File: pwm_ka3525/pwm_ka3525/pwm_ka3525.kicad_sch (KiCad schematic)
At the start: 17 parts, among them J1 shutdown, J2 Conn_01x03, J3 Conn_01x03, J4 Conn_01x02, U1 UC3525

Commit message: actualizacion
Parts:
- added C3: 0.1uF, Capacitor_THT:C_Disc_D7.5mm_W2.5mm_P5.00mm, symbol Device:C
- frec1: value 200k -> 150k
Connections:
- net +12V: now also C3.1
- net GND: now also C3.2
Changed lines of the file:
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@@
+    (stroke (width 0) (type default))
+  )
+  (wire (pts (xy 218.44 73.66) (xy 218.44 76.2))
     (stroke (width 0) (type default))
   )
@@
   )
   (wire (pts (xy 105.41 97.79) (xy 105.41 104.14))
+    (stroke (width 0) (type default))
+  )
+  (wire (pts (xy 218.44 83.82) (xy 218.44 85.09))
     (stroke (width 0) (type default))
   )
@@
         (path "/ea49c21e-f169-43d4-aeb6-478b59f13c59"
           (reference "#PWR09") (unit 1)
+        )
+      )
+    )
+  )
+  (symbol (lib_id "Device:C") (at 218.44 80.01 0) (unit 1)
+    (in_bom yes) (on_board yes) (dnp no) (fields_autoplaced)
+    (property "Reference" "C3" (at 222.25 79.375 0)
+      (effects (font (size 1.27 1.27)) (justify left))
+    )
+    (property "Value" "0.1uF" (at 222.25 81.915 0)
+      (effects (font (size 1.27 1.27)) (justify left))
+    )
+    (property "Footprint" "Capacitor_THT:C_Disc_D7.5mm_W2.5mm_P5.00mm" (at 219.4052 83.82 0)
+      (effects (font (size 1.27 1.27)) hide)
+    )
+    (property "Datasheet" "~" (at 218.44 80.01 0)
+      (effects (font (size 1.27 1.27)) hide)
+    )
+    (pin "1")
+    (pin "2")
+    (instances
+      (project "pwm_ka3525"
+        (path "/ea49c21e-f169-43d4-aeb6-478b59f13c59"
+          (reference "C3") (unit 1)
         )
       )
@@
     )
   )
+  (symbol (lib_id "power:GND") (at 218.44 85.09 0) (unit 1)
+    (in_bom yes) (on_board yes) (dnp no) (fields_autoplaced)
+    (property "Reference" "#PWR012" (at 218.44 91.44 0)
+      (effects (font (size 1.27 1.27)) hide)
+    )
+    (property "Value" "GND" (at 218.44 90.17 0)
+      (effects (font (size 1.27 1.27)))
+    )
+    (property "Footprint" "" (at 218.44 85.09 0)
+      (effects (font (size 1.27 1.27)) hide)
+    )
+    (property "Datasheet" "" (at 218.44 85.09 0)
+      (effects (font (size 1.27 1.27)) hide)
+    )
+    (pin "1")
+    (instances
+      (project "pwm_ka3525"
+        (path "/ea49c21e-f169-43d4-aeb6-478b59f13c59"
+          (reference "#PWR012") (unit 1)
+        )
+      )
+    )
+  )
+  (symbol (lib_id "power:+12V") (at 218.44 73.66 0) (unit 1)
+    (in_bom yes) (on_board yes) (dnp no) (fields_autoplaced)
+    (property "Reference" "#PWR013" (at 218.44 77.47 0)
+      (effects (font (size 1.27 1.27)) hide)
+    )
+    (property "Value" "+12V" (at 218.44 69.85 0)
+      (effects (font (size 1.27 1.27)))
+    )
+    (property "Footprint" "" (at 218.44 73.66 0)
+      (effects (font (size 1.27 1.27)) hide)
+    )
+    (property "Datasheet" "" (at 218.44 73.66 0)
+      (effects (font (size 1.27 1.27)) hide)
+    )
+    (pin "1")
+    (instances
+      (project "pwm_ka3525"
+        (path "/ea49c21e-f169-43d4-aeb6-478b59f13c59"
+          (reference "#PWR013") (unit 1)
+        )
+      )
+    )
+  )
   (symbol (lib_id "Device:R") (at 107.95 35.56 90) (unit 1)
     (in_bom yes) (on_board yes) (dnp no) (fields_autoplaced)
@@
       (effects (font (size 1.27 1.27)) (justify right))
     )
-    (property "Value" "200k" (at 102.87 112.395 0)
-      (effects (font (size 1.27 1.27)) (justify right))
-    )
+    (property "Value" "150k" (at 102.87 112.395 0)
+      (effects (font (size 1.27 1.27)) (justify right))
+    )

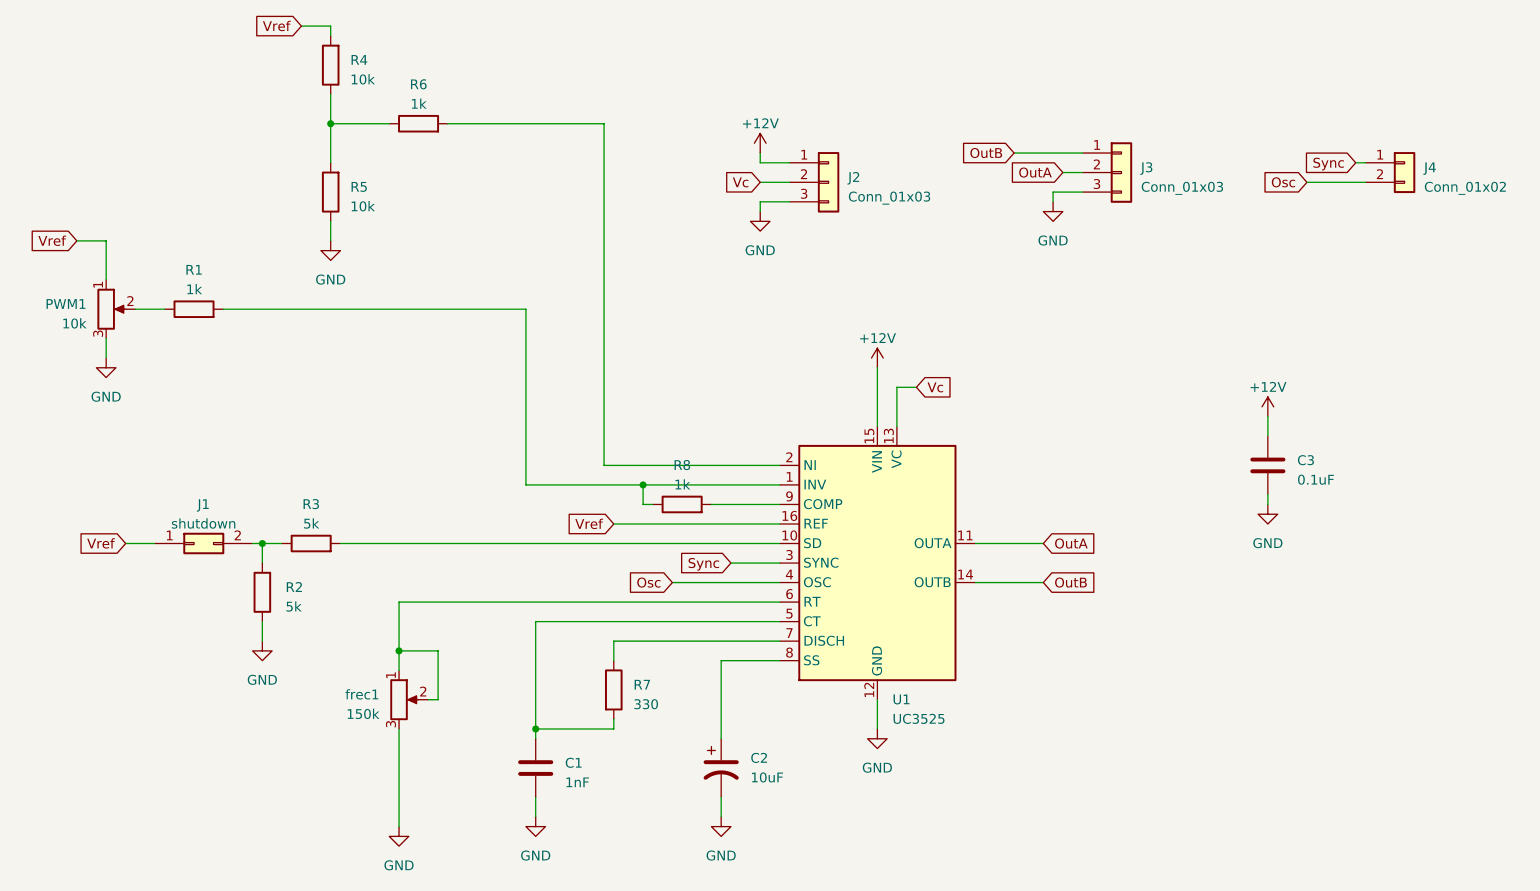
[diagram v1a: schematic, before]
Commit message: rediseño driver BJT
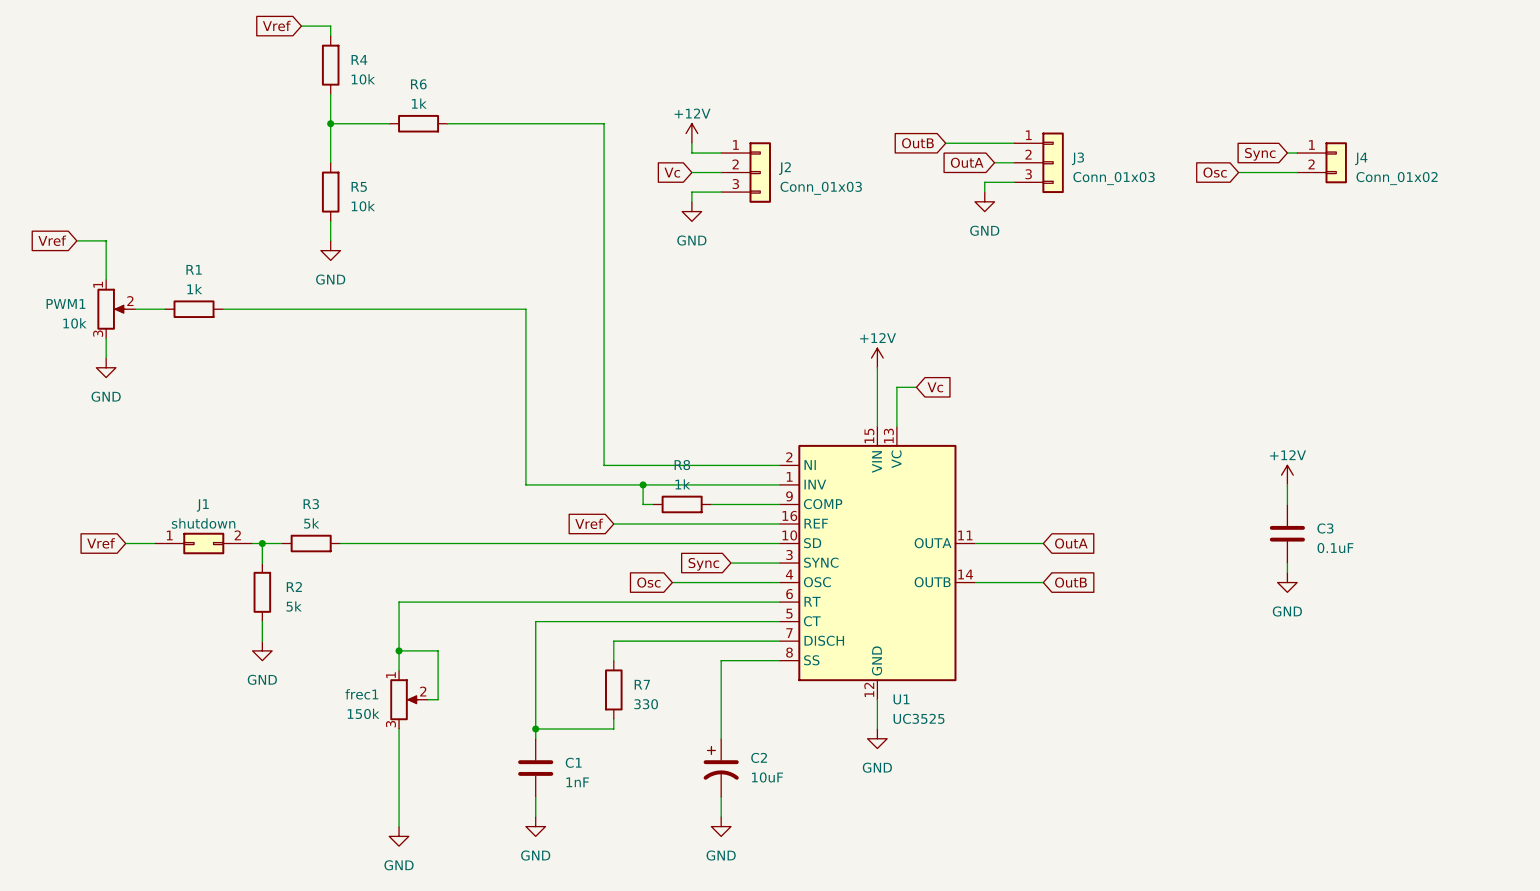
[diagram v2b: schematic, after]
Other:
- moved on the sheet: C3, J2, J3, J4
